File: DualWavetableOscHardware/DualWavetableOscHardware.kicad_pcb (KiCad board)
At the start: 4 copper layers, 50.8 x 110 mm, 81 parts, among them J101 CV1, J102 MOD1, J103 SWD Header, J104 POWER, J105 CV2, J106 MOD2, J107 OUT1, J108 OUT2, J109 Micro_SD_Card, SW101 RST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

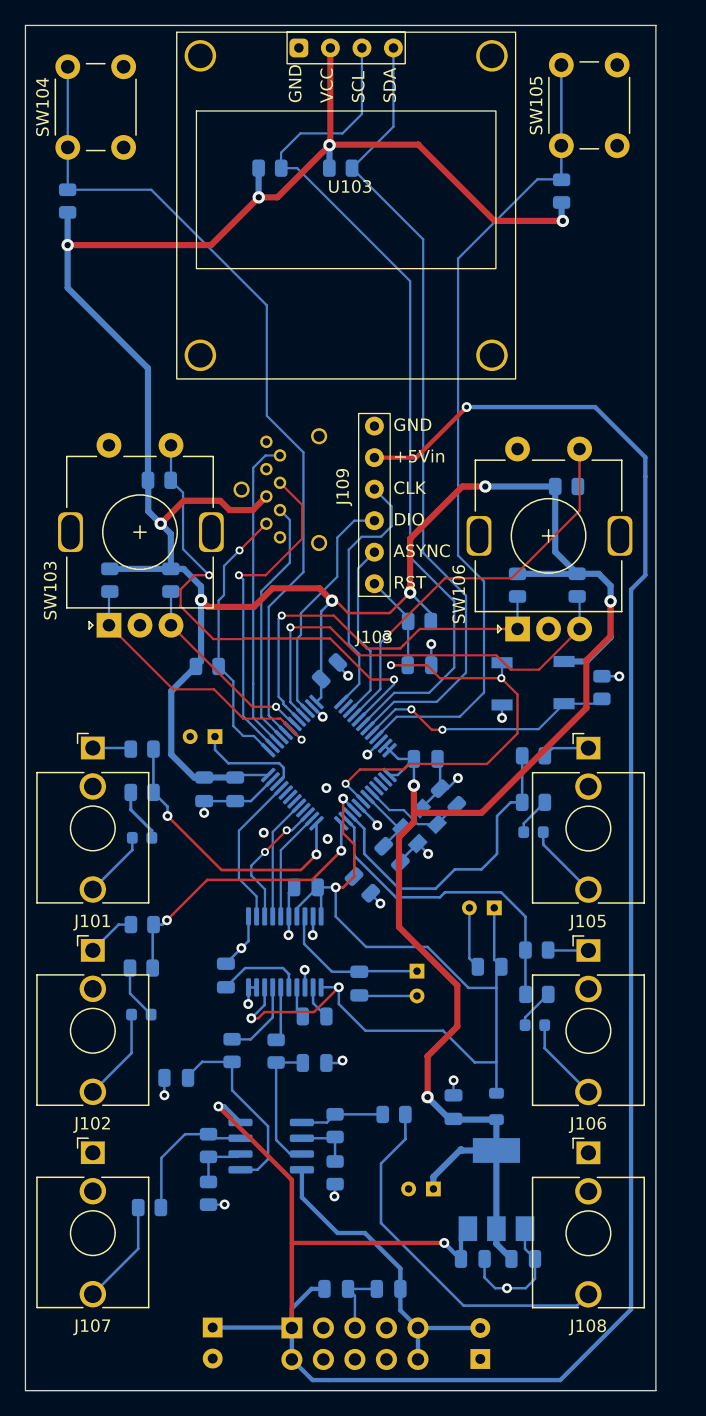
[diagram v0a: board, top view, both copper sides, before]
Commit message: double buffer for I2S
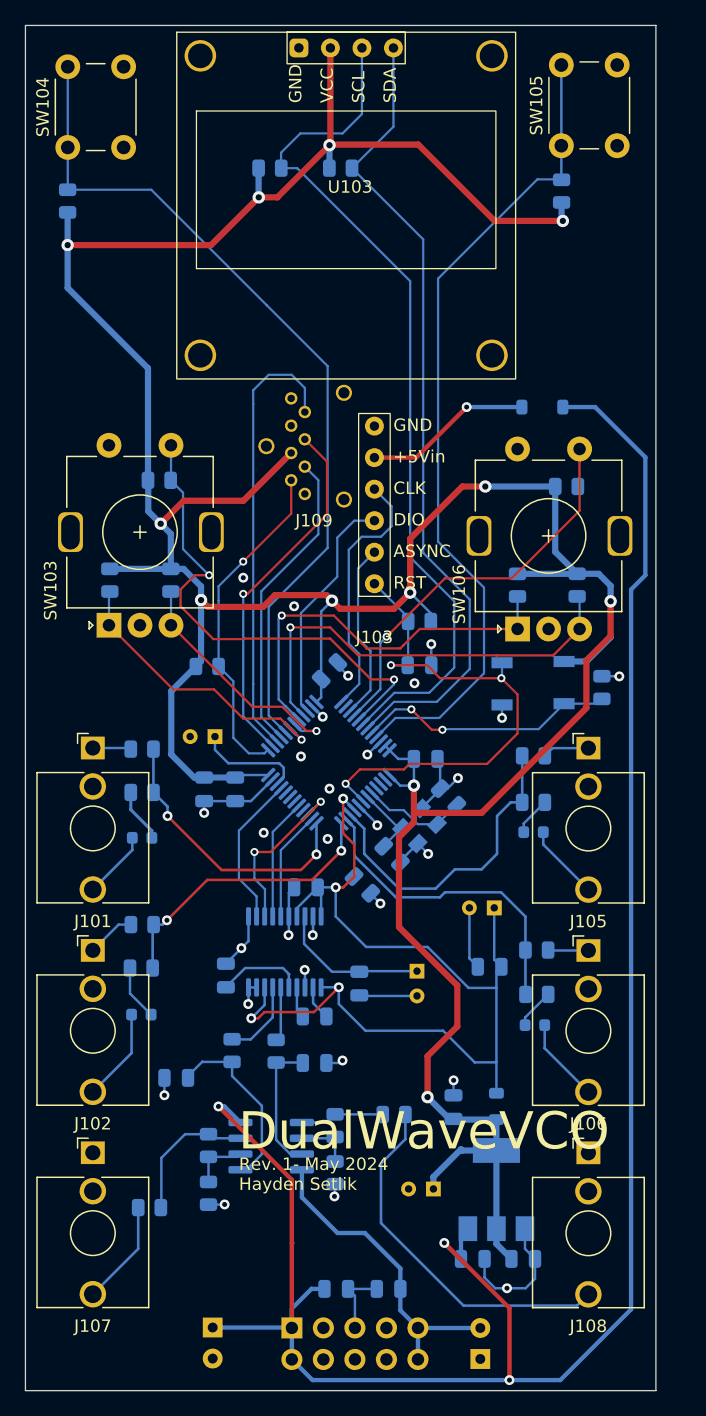
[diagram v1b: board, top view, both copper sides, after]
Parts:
- added D105: 1N4148, Diode_SMD:D_SOD-123, B.Cu at (41.6, 30.8)
- moved J109 4.03 mm to (28.6, 33.9)
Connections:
- J103 pad 2: +12V -> Net-(D105-A)
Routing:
- net +12V: track 177.9 -> 162.1 mm
- net Net-(D105-A): track 0.00 -> 13.6 mm, vias 0 -> 1
- net MISO: track 25.4 -> 36.1 mm
- net SD_CS: track 22.0 -> 27.1 mm
- net MOSI: track 20.2 -> 24.8 mm
- net ENC1_R: track 16.1 -> 20.1 mm
- net I2S_BCK: track 10.8 -> 14.1 mm
- net SCK: track 26.4 -> 29.4 mm
- net +3.3V: track 293.6 -> 296.4 mm
- net CH_BTN: track 67.2 -> 68.8 mm
- net Net-(U105B-+): track 15.8 -> 14.9 mm
- net ENC2_R: track 36.3 -> 35.3 mm
- net GND: vias 25 -> 29
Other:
- board text added: "BOOT0"
- board text added: "DualWaveVCO"
- board text added: "I2C pullup"
- board text added: "RST"
- board text added: "Rev. 1- May 2024 Hayden Setlik"

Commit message: status LEDs and test points
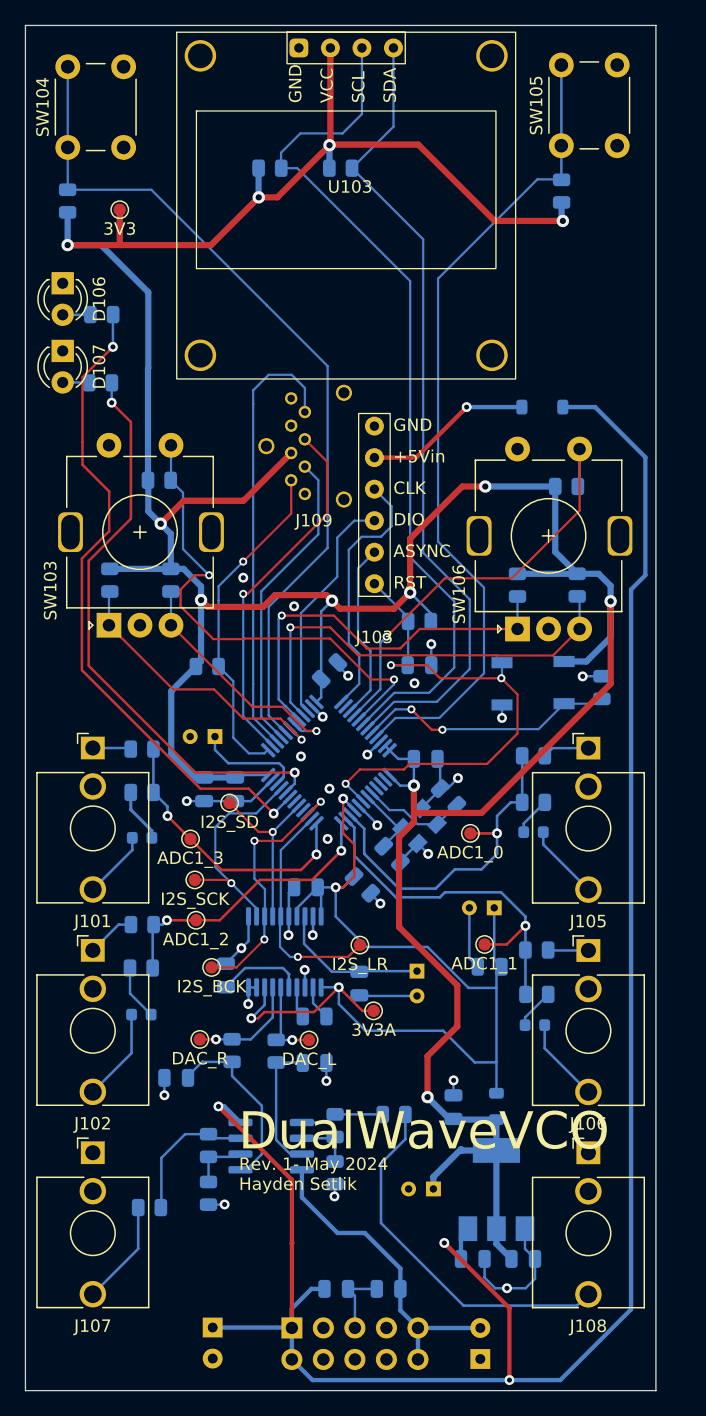
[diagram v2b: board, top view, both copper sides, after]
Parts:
- added D106: LED_GRN, LED_THT:LED_D3.0mm, F.Cu at (3.00, 20.8)
- added D107: LED_RED, LED_THT:LED_D3.0mm, F.Cu at (3.00, 26.2)
- added R130: 220, PCM_Resistor_SMD_AKL:R_0805_2012Metric, B.Cu at (6.15, 23.3)
- added R131: 220, PCM_Resistor_SMD_AKL:R_0805_2012Metric, B.Cu at (6.05, 28.8)
- added TP101: I2S_SCK, TestPoint:TestPoint_Pad_D1.0mm_Value, F.Cu at (13.7, 68.8)
- added TP102: I2S_BCK, TestPoint:TestPoint_Pad_D1.0mm_Value, F.Cu at (15.0, 75.9)
- added TP103: 3V3A, TestPoint:TestPoint_Pad_D1.0mm_Value, F.Cu at (28.1, 79.4)
- added TP104: 3V3, TestPoint:TestPoint_Pad_D1.0mm_Value, F.Cu at (7.60, 14.8)
- added TP105: DAC_R, TestPoint:TestPoint_Pad_D1.0mm_Value, F.Cu at (14.1, 81.7)
- added TP106: DAC_L, TestPoint:TestPoint_Pad_D1.0mm_Value, F.Cu at (22.9, 81.8)
- added TP107: ADC1_0, TestPoint:TestPoint_Pad_D1.0mm_Value, F.Cu at (35.9, 65.1)
- added TP108: ADC1_1, TestPoint:TestPoint_Pad_D1.0mm_Value, F.Cu at (37.0, 74.0)
- added TP109: I2S_SD, TestPoint:TestPoint_Pad_D1.0mm_Value, F.Cu at (16.4, 62.6)
- added TP110: I2S_LR, TestPoint:TestPoint_Pad_D1.0mm_Value, F.Cu at (26.9, 74.1)
- added TP111: ADC1_2, TestPoint:TestPoint_Pad_D1.0mm_Value, F.Cu at (13.8, 72.1)
- added TP112: ADC1_3, TestPoint:TestPoint_Pad_D1.0mm_Value, F.Cu at (13.3, 65.5)
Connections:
- U101 pad 19: unconnected-(U101-PB1-Pad19) -> LED_GRN
- U101 pad 20: unconnected-(U101-PB2-Pad20) -> LED_RED
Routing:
- net LED_GRN: track 0.00 -> 53.6 mm, vias 0 -> 2
- net LED_RED: track 0.00 -> 46.9 mm, vias 0 -> 2
- net I2S_WS: track 8.90 -> 18.5 mm, vias 0 -> 1
- net I2S_BCK: track 14.1 -> 21.6 mm, vias 2 -> 3
- net I2S_SCK: track 12.3 -> 18.2 mm, vias 0 -> 1
- net +3.3V: track 296.4 -> 300.9 mm
- net I2S_DIO: track 9.79 -> 14.2 mm, vias 0 -> 1
- net MOD2_ADC: track 25.7 -> 29.6 mm, vias 0 -> 1
- net +3.3VA: track 80.1 -> 83.7 mm
- net Net-(U104-OUTL): track 4.38 -> 7.04 mm, vias 0 -> 1
- net Net-(U104-OUTR): track 6.43 -> 9.03 mm, vias 0 -> 1
- net Net-(D106-A): track 0.00 -> 2.24 mm
- net Net-(D107-A): track 0.00 -> 2.15 mm
- net CV2_ADC: track 25.9 -> 28.1 mm, vias 0 -> 1
- net GND: track 88.6 -> 89.2 mm, vias 29 -> 28

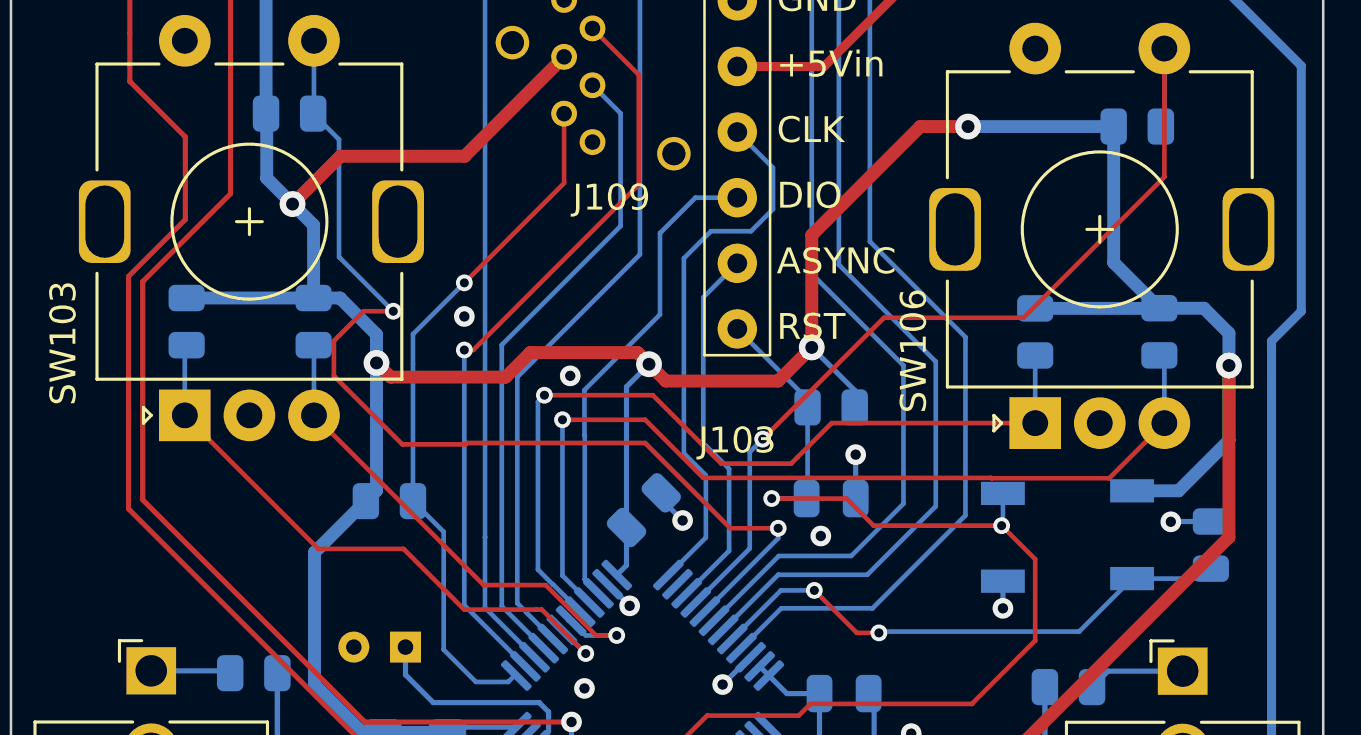
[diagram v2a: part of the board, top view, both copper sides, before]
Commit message: status LED code
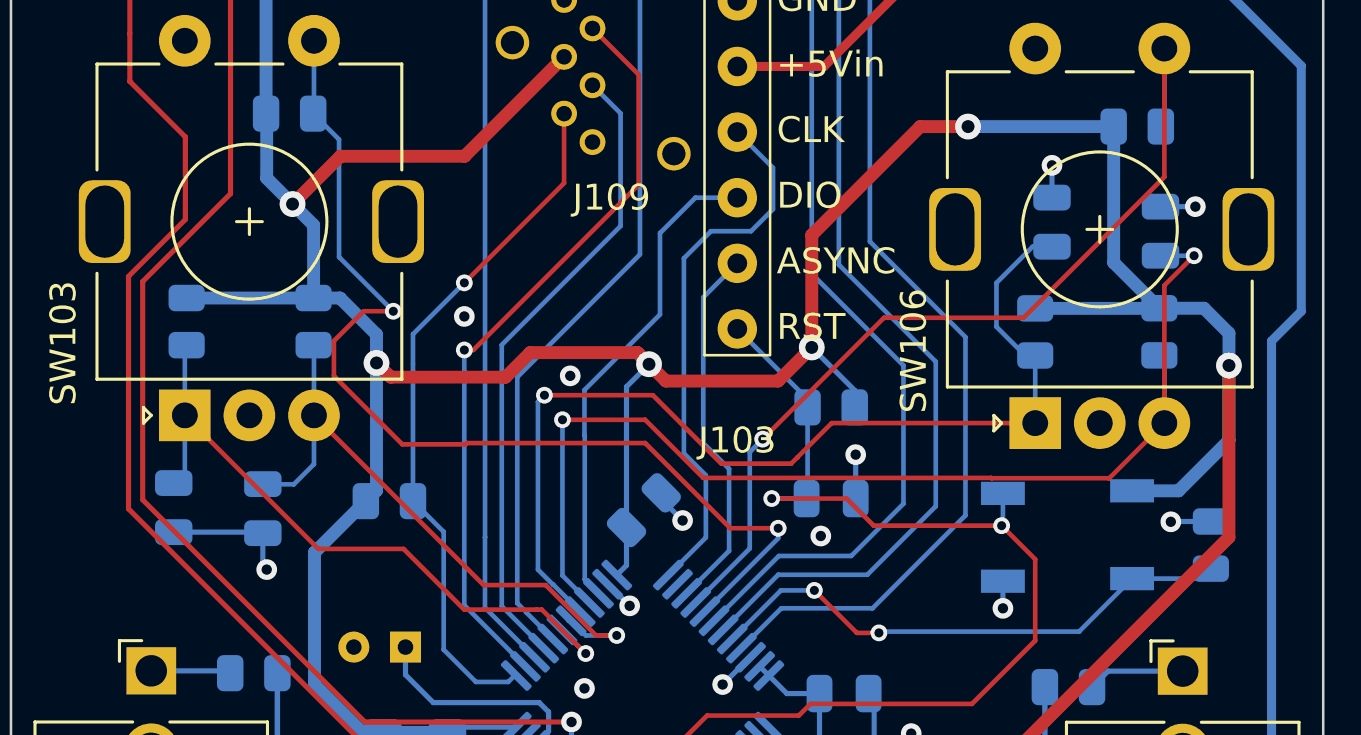
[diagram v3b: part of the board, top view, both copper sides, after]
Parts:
- added C127: 100n, Capacitor_SMD:C_0805_2012Metric, B.Cu at (9.75, 51.9)
- added C128: 100n, Capacitor_SMD:C_0805_2012Metric, B.Cu at (6.30, 51.9)
- added C129: 100n, Capacitor_SMD:C_0805_2012Metric, B.Cu at (44.5, 41.2)
- added C130: 100n, Capacitor_SMD:C_0805_2012Metric, B.Cu at (40.3, 40.9)
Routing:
- net ENC2_R: track 35.3 -> 43.6 mm, vias 1 -> 2
- net GND: track 89.2 -> 96.8 mm, vias 28 -> 31
- net ENC2_L: track 32.5 -> 38.9 mm
- net ENC1_R: track 20.1 -> 24.3 mm
- net ENC1_L: track 23.4 -> 26.2 mm

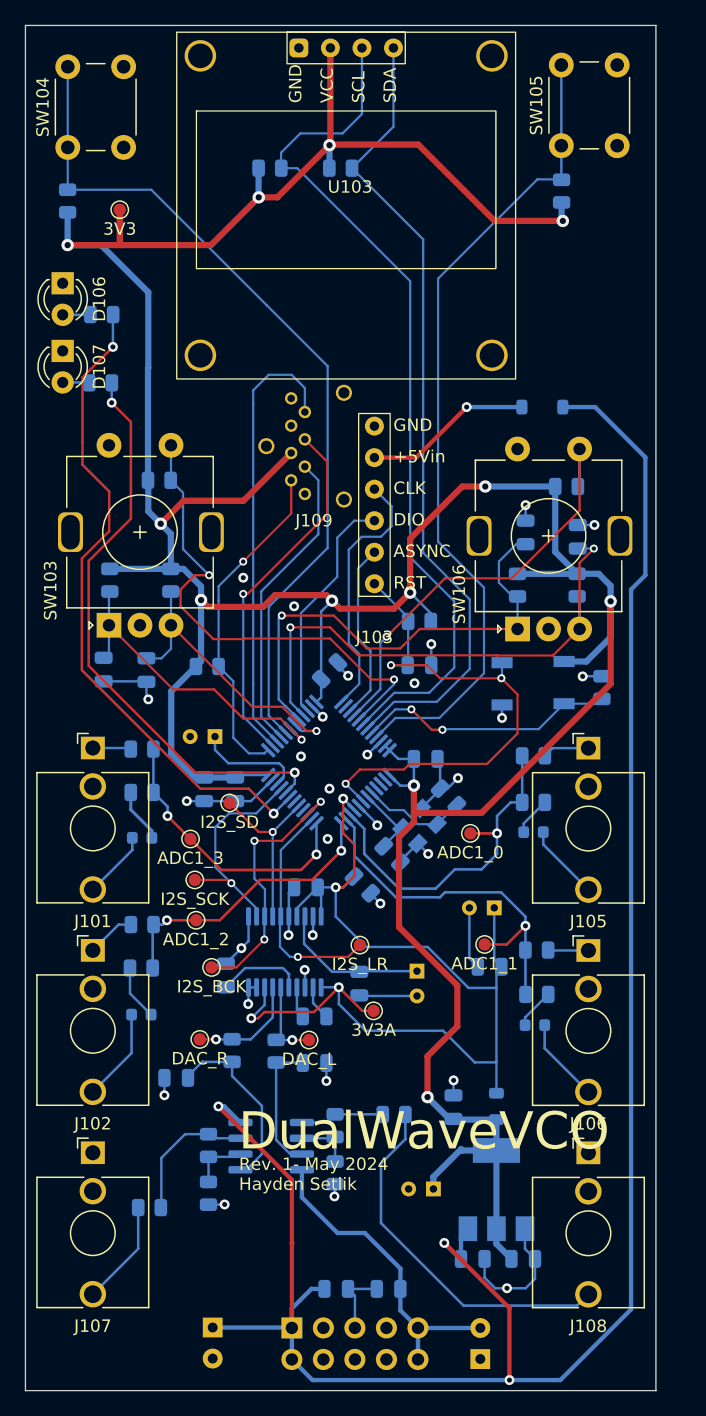
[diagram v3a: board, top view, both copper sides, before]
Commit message: new stackup/routing
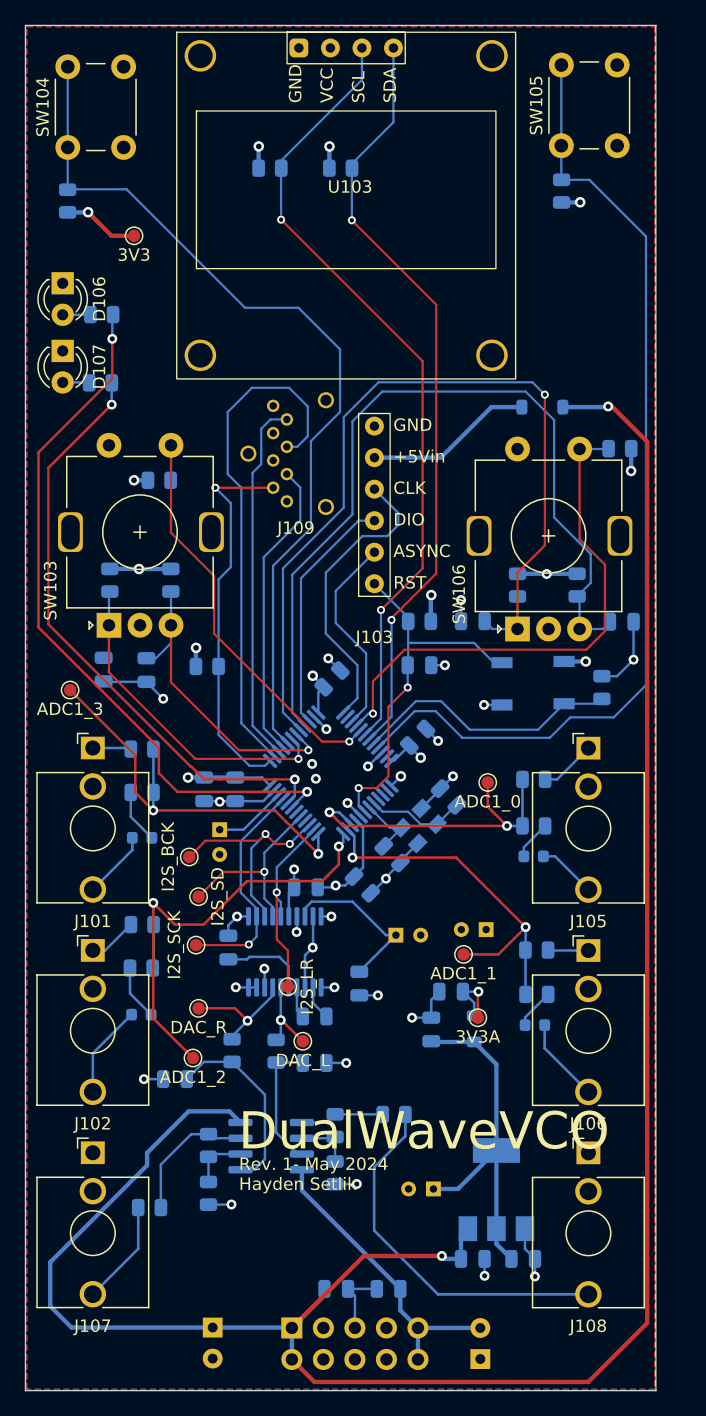
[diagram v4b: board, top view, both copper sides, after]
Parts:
- moved TP112 15.4 mm to (3.60, 53.5)
- moved TP111 11.1 mm to (13.5, 83.2)
- moved TP102 9.08 mm to (13.2, 67.0)
- moved TP103 8.42 mm to (36.5, 80.0)
- moved C130 8.32 mm to (36.0, 48.0), turned to 0 degrees
- moved TP109 7.95 mm to (13.9, 70.2), turned to 90 degrees
- moved C129 7.72 mm to (48.0, 48.0), turned to 180 degrees
- moved C111 7.51 mm to (15.7, 64.8), turned to -90 degrees
- moved TP110 6.70 mm to (21.1, 77.5), turned to 90 degrees
- moved FB101 6.51 mm to (36.2, 80.8)
- moved C118 6.51 mm to (32.7, 80.9)
- moved R120 5.27 mm to (47.9, 34.1), turned to 180 degrees
- moved TP101 5.25 mm to (13.8, 74.1)
- moved TP107 4.33 mm to (37.2, 61.0)
- moved C116 3.69 mm to (34.3, 77.8)
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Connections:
- net Net-(D105-A) renamed VCC_DEBUG
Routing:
- net +3.3V: track 300.9 -> 73.1 mm, vias 12 -> 15
- net +3.3VA: track 83.7 -> 18.9 mm, vias 4 -> 6
- net ENC2_L: track 38.9 -> 71.0 mm
- net ENC2_R: track 43.6 -> 66.4 mm, vias 2 -> 0
- net +12V: track 162.1 -> 181.0 mm, vias 3 -> 2
- net MOD1_ADC: track 23.3 -> 39.4 mm
- net MODE_BTN: track 66.7 -> 79.5 mm
- net SCK: track 29.4 -> 41.6 mm, vias 1 -> 0
- net NRST: track 42.2 -> 30.5 mm, vias 3 -> 2
- net CV1_ADC: track 22.7 -> 33.8 mm
- net ENC2_B: track 35.2 -> 42.6 mm
- net MISO: track 36.1 -> 29.6 mm
- net SCL: track 70.4 -> 64.7 mm, vias 0 -> 2
- net GND: track 96.8 -> 91.1 mm, vias 31 -> 27
- net ENC1_B: track 40.0 -> 35.2 mm, vias 2 -> 1
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- added copper zone on In1.Cu, net +3.3V
- added copper zone on In1.Cu, net +3.3VA
- added copper zone on B.Cu, net GND
- added copper zone on F.Cu, net GND
- removed copper zone on In1.Cu, net GND

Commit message: wavetable generation
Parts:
- moved C117 9.84 mm to (37.9, 85.3)
- moved TP104 2.45 mm to (7.20, 15.1)
- moved TP108 2.22 mm to (37.5, 75.2)
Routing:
- net GND: track 91.1 -> 83.3 mm, vias 27 -> 28
- net +3.3V: track 73.1 -> 66.7 mm
- net ENC2_L: track 71.0 -> 73.7 mm
- net MOD2_ADC: track 30.2 -> 28.8 mm
- net SD_CS: track 30.8 -> 29.8 mm
